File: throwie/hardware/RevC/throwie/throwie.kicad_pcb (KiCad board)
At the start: 2 copper layers, 33.8 x 18.8 mm, 30 parts, among them J1 CONN, Q1 2SC3356, Q2 SS8050-G, T0 TestPoints, T1 TestPoints, T2 TestPoints, T3 TestPoints, T4 TestPoints, T5 TestPoints, T6 TestPoints, T7 TestPoints, T8 TestPoints, T9 TestPoints, U1 C8051F850-A-GU, U2 MIC5231-3.3YM5-TR, X1 RO3101

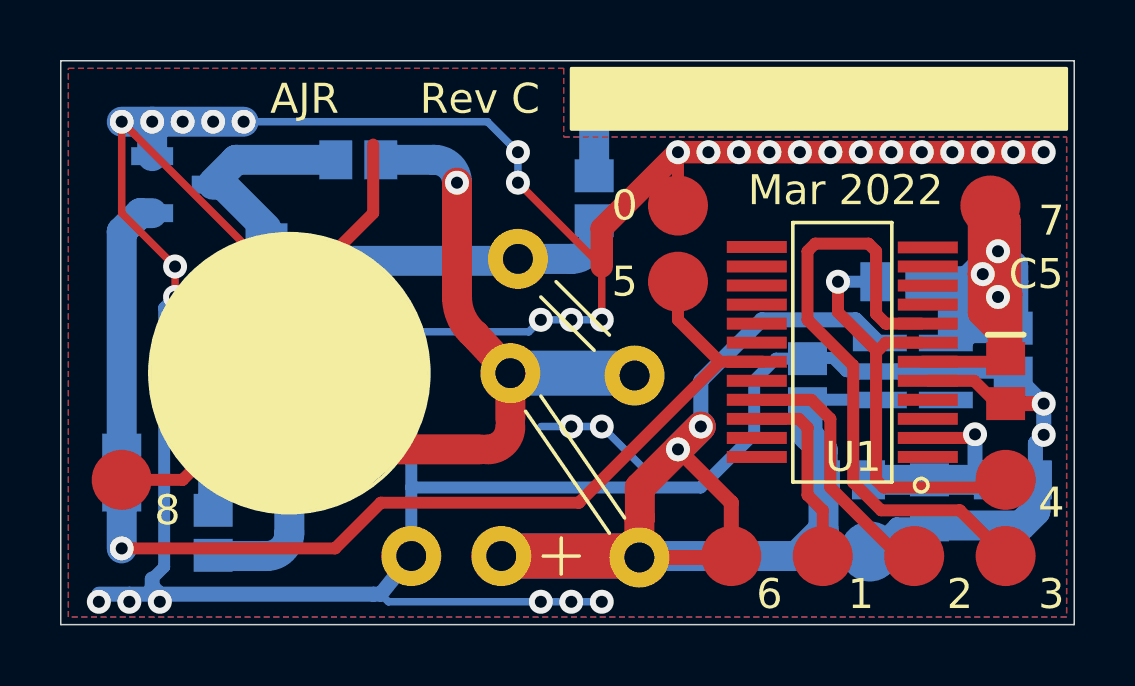
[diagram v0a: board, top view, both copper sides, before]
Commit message: adjust floods
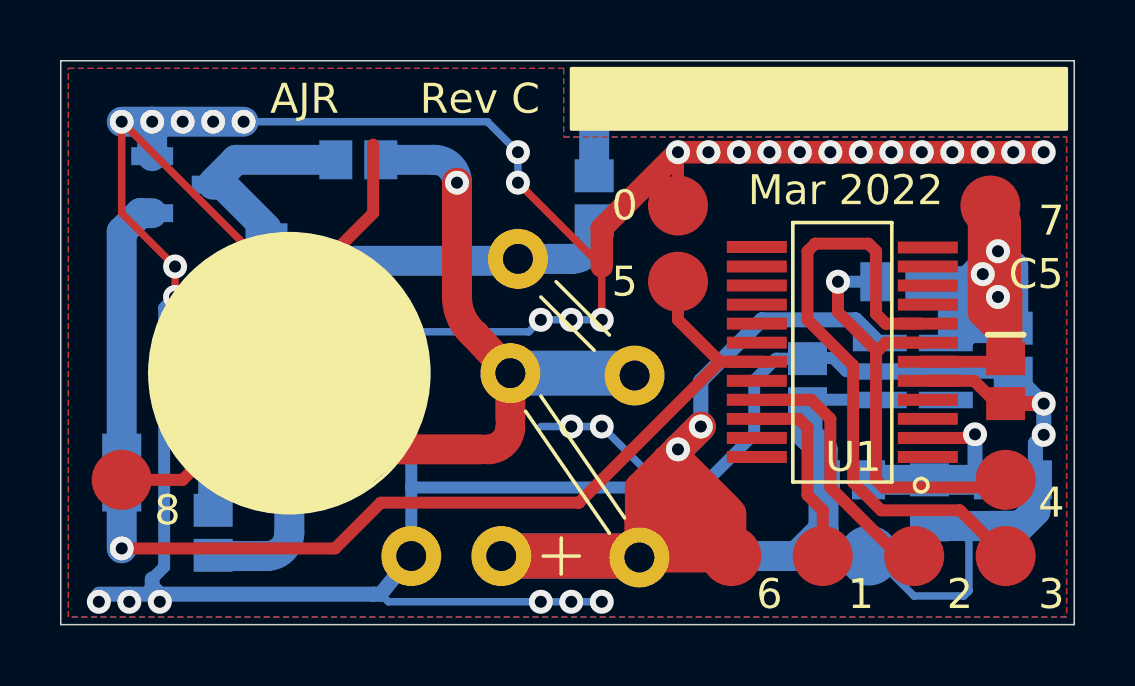
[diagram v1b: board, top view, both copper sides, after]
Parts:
- moved T9 0.14 mm to (47.5, 161.0)
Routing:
- net +BATT: track 49.1 -> 70.0 mm
- net GNDREF: track 161.2 -> 166.4 mm
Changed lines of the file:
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@@
     (thickness 1.6)
     (drawings 40)
-    (tracks 292)
+    (tracks 320)
     (zones 0)
     (modules 30)
@@
   (layers
     (0 F.Cu signal)
-    (31 B.Cu signal)
+    (31 B.Cu signal hide)
     (32 B.Adhes user hide)
-    (33 F.Adhes user)
+    (33 F.Adhes user hide)
     (34 B.Paste user hide)
     (35 F.Paste user hide)
     (36 B.SilkS user hide)
-    (37 F.SilkS user)
+    (37 F.SilkS user hide)
     (38 B.Mask user hide)
     (39 F.Mask user hide)
@@
     (42 Eco1.User user hide)
     (43 Eco2.User user hide)
-    (44 Edge.Cuts user)
+    (44 Edge.Cuts user hide)
     (45 Margin user hide)
     (46 B.CrtYd user hide)
@@
   )
   (setup
-    (last_trace_width 0.5)
+    (last_trace_width 1)
     (user_trace_width 0.4)
     (user_trace_width 0.5)
@@
   )
   (module throwie:TestPoint (layer B.Cu)
-    (at 47.54372 160.8836)
+    (at 47.51324 161.02076)
     (fp_text reference T9 (at 0 -0.5) (layer B.SilkS) hide
       (effects (font (size 1 1) (thickness 0.15)) (justify mirror))
@@
   (module throwie:0603 (layer B.Cu)
     (at 45.998 158.496)
-    (fp_text reference R2 (at 0.738 1.778) (layer B.SilkS)
+    (fp_text reference R2 (at -1.8274 1.55956) (layer B.SilkS)
       (effects (font (size 1 1) (thickness 0.15)) (justify mirror))
     )
@@
   (module throwie:0603 (layer B.Cu)
     (at 49.53 158.496 270)
-    (fp_text reference C6 (at 3.048 0 180) (layer B.SilkS)
+    (fp_text reference C6 (at 2.97688 -0.5842 180) (layer B.SilkS)
       (effects (font (size 1 1) (thickness 0.15)) (justify mirror))
     )
@@
     (effects (font (size 1 1) (thickness 0.15)))
   )
-  (gr_text 9 (at 46.16704 162.02152) (layer B.SilkS)
+  (gr_text 9 (at 45.92828 162.23996) (layer B.SilkS)
     (effects (font (size 1 1) (thickness 0.15)))
   )
@@
   (segment (start 53.062 158.496) (end 53.062 159.536) (width 1) (layer B.Cu) (net 2))
   (segment (start 53.062 159.536) (end 52.578 160.02) (width 1) (layer B.Cu) (net 2))
-  (segment (start 52.578 160.02) (end 49.53 160.02) (width 1) (layer B.Cu) (net 2))
   (segment (start 53.086 158.032826) (end 53.086 158.496) (width 0.5) (layer B.Cu) (net 2))
   (segment (start 48.26 154.874) (end 52.258 154.874) (width 0.5) (layer B.Cu) (net 2))
@@
   (segment (start 45.49 154.432) (end 45.466 154.456) (width 0.4) (layer B.Cu) (net 2))
   (segment (start 46.318 154.432) (end 45.49 154.432) (width 0.4) (layer B.Cu) (net 2))
-  (segment (start 48.43132 159.996) (end 47.54372 160.8836) (width 0.5) (layer B.Cu) (net 2))
-  (segment (start 49.53 159.996) (end 48.43132 159.996) (width 0.5) (layer B.Cu) (net 2))
+  (segment (start 50.8014 159.996) (end 50.84572 160.04032) (width 0.25) (layer B.Cu) (net 2))
+  (segment (start 49.53 159.996) (end 50.8014 159.996) (width 0.25) (layer B.Cu) (net 2))
+  (segment (start 50.84572 160.04032) (end 49.53 160.02) (width 1) (layer B.Cu) (net 2))
+  (segment (start 52.578 160.02) (end 50.84572 160.04032) (width 1) (layer B.Cu) (net 2))
+  (segment (start 50.84572 160.04032) (end 50.84572 162.19932) (width 0.25) (layer B.Cu) (net 2))
+  (segment (start 50.84572 162.19932) (end 50.67808 162.36696) (width 0.25) (layer B.Cu) (net 2))
+  (segment (start 49.01692 162.36696) (end 47.5234 160.87344) (width 0.25) (layer B.Cu) (net 2))
+  (segment (start 50.67808 162.36696) (end 49.01692 162.36696) (width 0.25) (layer B.Cu) (net 2))
   (segment (start 40.352 161.036) (end 39.878 161.036) (width 0.4) (layer B.Cu) (net 3))
   (segment (start 40.674 161.036) (end 39.878 161.036) (width 0.4) (layer B.Cu) (net 3))
@@
   (segment (start 43.18 160.782) (end 42.926 161.036) (width 0.4) (layer F.Cu) (net 3))
   (segment (start 42.926 161.036) (end 42.418 161.036) (width 0.4) (layer F.Cu) (net 3))
-  (segment (start 42.87836 161.08364) (end 42.926 161.036) (width 0.5) (layer F.Cu) (net 3))
-  (segment (start 39.861823 161.08364) (end 42.87836 161.08364) (width 0.5) (layer F.Cu) (net 3))
-  (segment (start 42.926 159.258) (end 41.148 157.48) (width 0.5) (layer F.Cu) (net 3))
-  (segment (start 42.926 161.036) (end 42.926 159.258) (width 0.5) (layer F.Cu) (net 3))
   (segment (start 41.148 157.48) (end 41.91 156.718) (width 1) (layer B.Cu) (net 3))
-  (segment (start 41.91 156.718) (end 39.878 158.75) (width 1) (layer F.Cu) (net 3))
   (segment (start 45.598 155.824) (end 45.466 155.956) (width 0.4) (layer B.Cu) (net 3))
   (segment (start 48.06 155.824) (end 45.598 155.824) (width 0.4) (layer B.Cu) (net 3))
@@
   (segment (start 47.835 153.924) (end 47.073 153.162) (width 0.5) (layer B.Cu) (net 3))
   (segment (start 41.91 156.718) (end 41.91 155.194) (width 0.5) (layer B.Cu) (net 3))
+  (segment (start 42.926 159.258) (end 41.148 157.48) (width 0.25) (layer F.Cu) (net 3))
+  (segment (start 41.1734 157.84068) (end 42.83456 159.50184) (width 1) (layer F.Cu) (net 3))
+  (segment (start 40.78732 157.84068) (end 41.1734 157.84068) (width 1) (layer F.Cu) (net 3))
+  (segment (start 42.83456 159.50184) (end 42.926 159.258) (width 0.5) (layer F.Cu) (net 3))
+  (segment (start 41.91 156.718) (end 40.78732 157.84068) (width 1) (layer F.Cu) (net 3))
+  (segment (start 40.78732 157.84068) (end 39.878 158.75) (width 1) (layer F.Cu) (net 3))
+  (segment (start 42.806053 159.50184) (end 42.79392 159.50184) (width 1) (layer F.Cu) (net 3))
+  (segment (start 42.926 159.621787) (end 42.806053 159.50184) (width 1) (layer F.Cu) (net 3))
+  (segment (start 42.926 161.036) (end 42.926 159.621787) (width 1) (layer F.Cu) (net 3))
+  (segment (start 42.79392 159.50184) (end 42.83456 159.50184) (width 0.5) (layer F.Cu) (net 3))
+  (segment (start 41.1226 158.76016) (end 42.15892 159.79648) (width 1) (layer F.Cu) (net 3))
+  (segment (start 40.65016 158.76016) (end 41.1226 158.76016) (width 1) (layer F.Cu) (net 3))
+  (segment (start 42.926 161.036) (end 42.15892 159.79648) (width 1) (layer F.Cu) (net 3))
+  (segment (start 42.87836 161.08364) (end 42.926 161.036) (width 1) (layer F.Cu) (net 3))
+  (segment (start 39.861823 161.08364) (end 42.87836 161.08364) (width 1) (layer F.Cu) (net 3))
+  (segment (start 41.1226 159.822863) (end 41.1226 158.76016) (width 1) (layer F.Cu) (net 3))
+  (segment (start 41.148 158.496) (end 39.878 159.766) (width 1) (layer F.Cu) (net 3))
+  (segment (start 41.148 157.48) (end 41.148 158.496) (width 1) (layer F.Cu) (net 3))
+  (segment (start 41.1226 159.822863) (end 41.817577 160.51784) (width 1) (layer F.Cu) (net 3))
+  (segment (start 42.40784 160.51784) (end 42.926 161.036) (width 1) (layer F.Cu) (net 3))
+  (segment (start 41.817577 160.51784) (end 42.40784 160.51784) (width 1) (layer F.Cu) (net 3))
+  (segment (start 40.32312 161.08364) (end 40.92956 160.4772) (width 1) (layer F.Cu) (net 3))
+  (segment (start 39.861823 161.08364) (end 40.32312 161.08364) (width 1) (layer F.Cu) (net 3))
+  (segment (start 40.92956 160.4772) (end 41.1226 159.822863) (width 1) (layer F.Cu) (net 3))
+  (segment (start 40.597486 160.51784) (end 39.861823 159.782177) (width 1) (layer F.Cu) (net 3))
+  (segment (start 41.817577 160.51784) (end 40.597486 160.51784) (width 1) (layer F.Cu) (net 3))
+  (segment (start 41.148 159.797463) (end 39.861823 161.08364) (width 1) (layer F.Cu) (net 3))
+  (segment (start 41.148 157.48) (end 41.148 159.797463) (width 1) (layer F.Cu) (net 3))
   (segment (start 49.276 154.559) (end 51.943 154.559) (width 0.4) (layer F.Cu) (net 4))
   (segment (start 51.943 154.559) (end 52.07 154.432) (width 0.4) (layer F.Cu) (net 4))
@@
     (polygon
       (pts
-        (xy 52.832 161.29) (xy 41.148 161.29) (xy 41.402 159.258) (xy 52.578 158.496)
+        (xy 52.832 161.29) (xy 43.42384 161.27984) (xy 43.3832 159.21736) (xy 52.578 158.496)
       )
     )
@@
       )
     )
+  )
+  (zone (net 0) (net_name "") (layer B.Cu) (hatch edge 0.508)
+    (connect_pads (clearance 0.254))
+    (min_thickness 0.254)
+    (keepout (tracks allowed) (vias allowed) (copperpour not_allowed))
+    (fill (arc_segments 32) (thermal_gap 0.508) (thermal_bridge_width 0.508))
+    (polygon
+      (pts
+        (xy 33.5534 160.30448) (xy 34.27984 160.31464) (xy 34.27476 161.66084) (xy 34.30524 161.7726) (xy 33.55848 161.7472)
+        (xy 33.54832 160.2994)
+      )
+    )
